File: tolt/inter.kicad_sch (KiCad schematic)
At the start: 51 parts, among them U2 L6491, U3 L6491, U4 L6491

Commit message: yaaaaaaa
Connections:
- net GND: no longer C15.2, C17.2, C19.2
- net Ph_a: now also C15.2
- net Ph_b: now also C17.2
- net Ph_c: now also C19.2

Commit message: some fixed and edit
tbd : phase voltage sensing and adct1 wiring and add on/off switch
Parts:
- D1, D2, D3: now not fitted
- R1, R2, R3: now fitted
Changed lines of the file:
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@@
 		(in_bom yes)
 		(on_board yes)
-		(dnp yes)
+		(dnp no)
 		(fields_autoplaced yes)
 		(property "Reference" "R1"
@@
 		(in_bom yes)
 		(on_board yes)
-		(dnp yes)
+		(dnp no)
 		(fields_autoplaced yes)
 		(property "Reference" "R3"
@@
 		(in_bom yes)
 		(on_board yes)
-		(dnp no)
+		(dnp yes)
 		(fields_autoplaced yes)
 		(property "Reference" "D3"
@@
 		(in_bom yes)
 		(on_board yes)
-		(dnp no)
+		(dnp yes)
 		(fields_autoplaced yes)
 		(property "Reference" "D2"
@@
 		(in_bom yes)
 		(on_board yes)
-		(dnp yes)
+		(dnp no)
 		(fields_autoplaced yes)
 		(property "Reference" "R2"
@@
 		(in_bom yes)
 		(on_board yes)
-		(dnp no)
+		(dnp yes)
 		(fields_autoplaced yes)
 		(property "Reference" "D1"

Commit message: idk just pushed for github profile lol
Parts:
- added TP1, TP2, TP3, TP4, TP5, TP6, TP7, TP8, TP9: TestPoint, symbol Connector:TestPoint
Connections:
- net H_A: now also TP3.1
- net H_B: now also TP2.1
- net H_C: now also TP5.1
- net L_A: now also TP4.1
- net L_B: now also TP1.1
- net L_C: now also TP6.1
- net SENS_A+: now also TP9.1
- net SENS_B+: now also TP8.1
- net SENS_C+: now also TP7.1

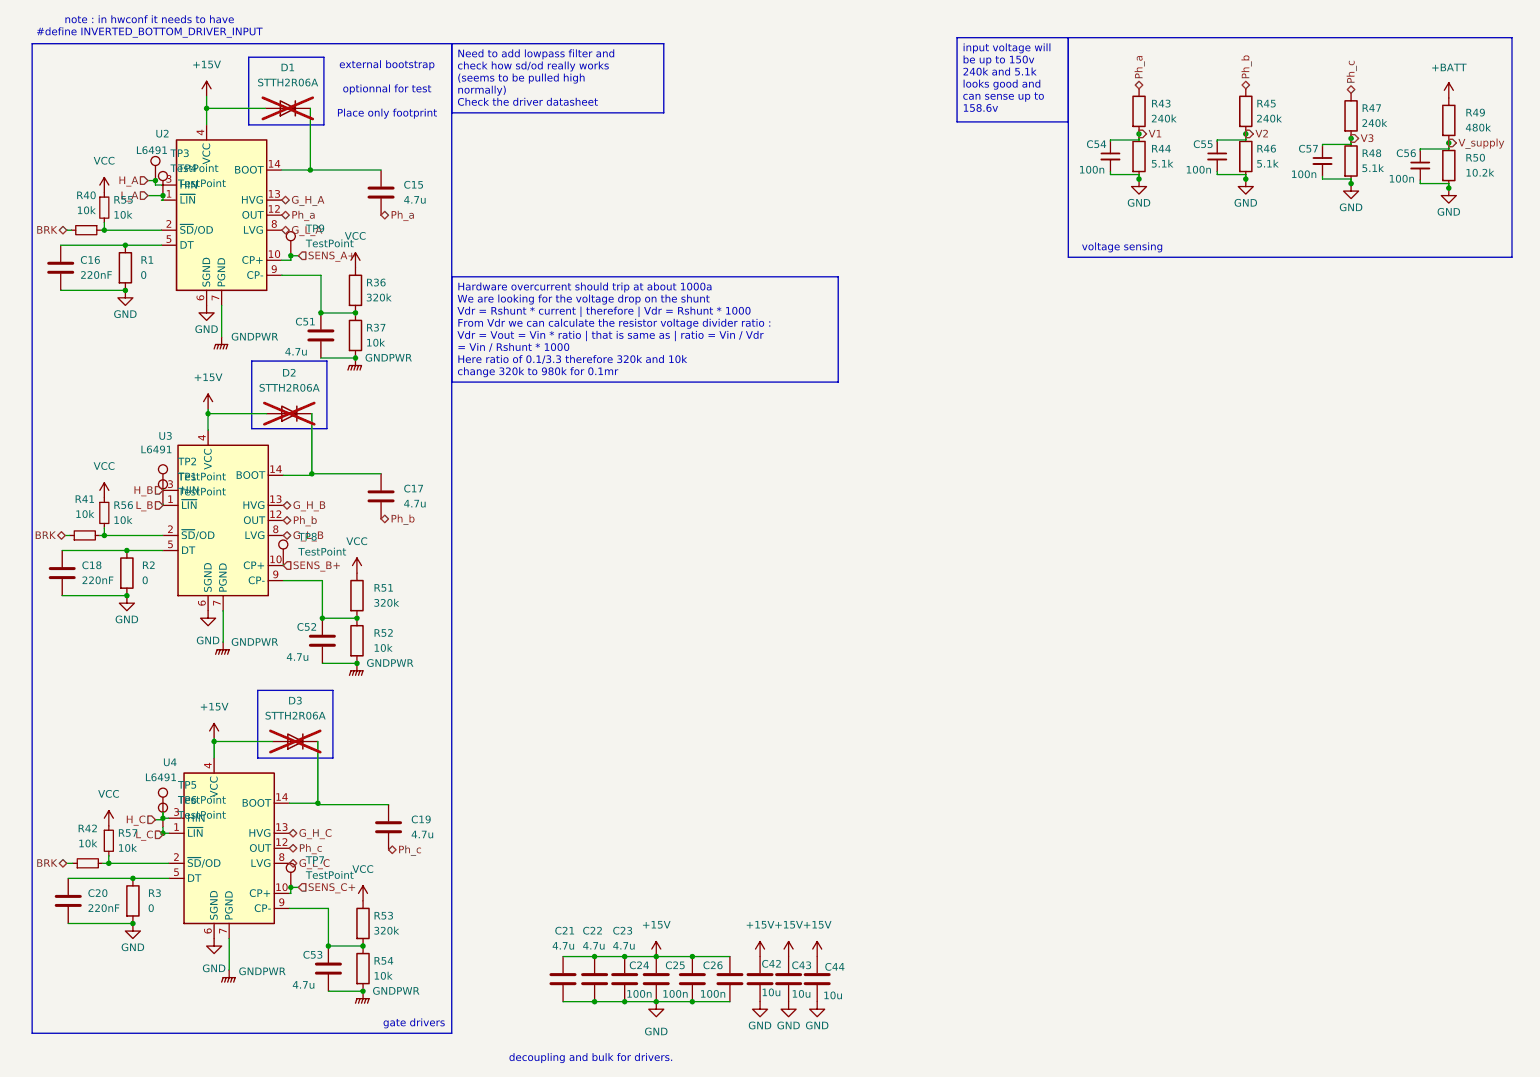
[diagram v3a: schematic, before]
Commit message: big update
fixed decoupling correctly
more gnd plane work and routing finished
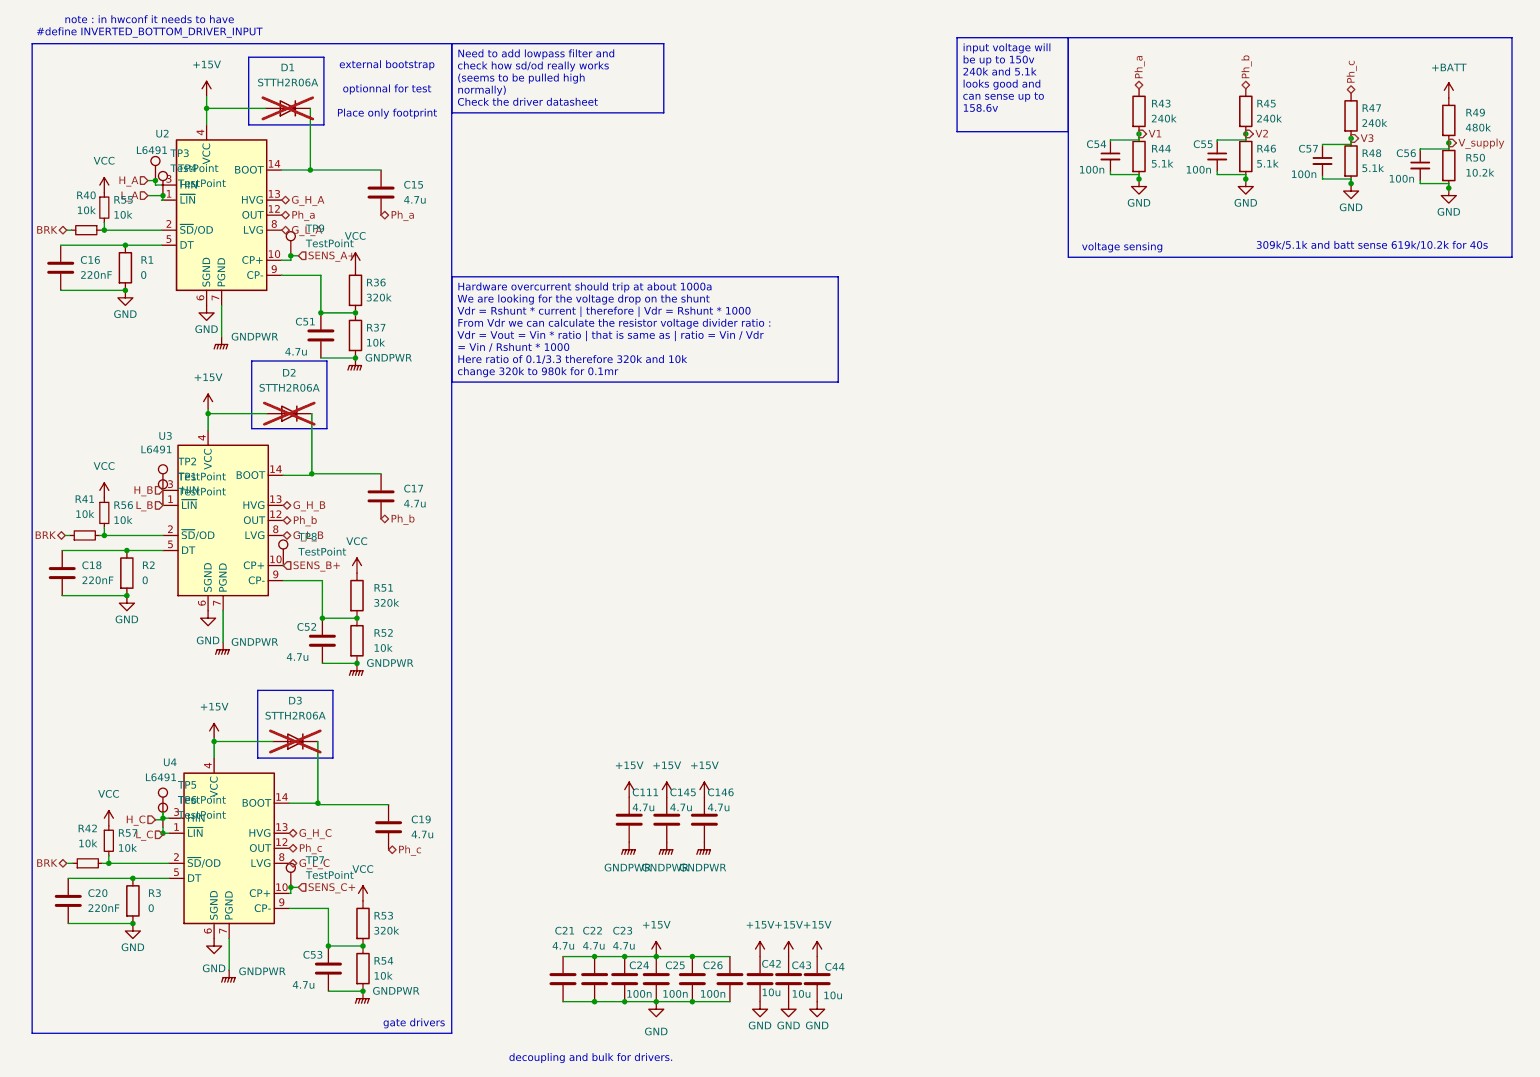
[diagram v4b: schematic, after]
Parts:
- added C111, C145, C146: 4.7u, Capacitor_SMD:C_0805_2012Metric, symbol Device:C
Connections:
- net +15V: now also C111.2, C145.2, C146.2
- net GNDPWR: now also C111.1, C145.1, C146.1
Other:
- note added: "309k/5.1k and batt sense 619k/10.2k for 40s"

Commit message: begenning of lcsc part assign
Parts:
- C42, C43, C44: footprint Capacitor_SMD:C_1210_3225Metric_Pad1.33x2.70mm_HandSolder -> Capacitor_SMD:C_1210_3225Metric
- R37, R52, R54: LCSC (none) -> C25804
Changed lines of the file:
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@@
 			)
 		)
-		(property "Footprint" "Capacitor_SMD:C_1210_3225Metric_Pad1.33x2.70mm_HandSolder"
+		(property "Footprint" "Capacitor_SMD:C_1210_3225Metric"
 			(at 156.1592 181.864 0)
 			(effects
@@
 			)
 		)
+		(property "LCSC" "C25804"
+			(at 83.312 176.276 0)
+			(effects
+				(font
+					(size 1.27 1.27)
+				)
+				(hide yes)
+			)
+		)
 		(pin "2"
 		)
@@
 			)
 		)
-		(property "Footprint" "Capacitor_SMD:C_1210_3225Metric_Pad1.33x2.70mm_HandSolder"
+		(property "Footprint" "Capacitor_SMD:C_1210_3225Metric"
 			(at 160.9852 181.864 0)
 			(effects
@@
 			)
 		)
+		(property "LCSC" "C25804"
+			(at 82.296 120.904 0)
+			(effects
+				(font
+					(size 1.27 1.27)
+				)
+				(hide yes)
+			)
+		)
 		(pin "2"
 		)
@@
 			)
 		)
+		(property "LCSC" "C25804"
+			(at 82.042 69.342 0)
+			(effects
+				(font
+					(size 1.27 1.27)
+				)
+				(hide yes)
+			)
+		)
 		(pin "2"
 		)
@@
 			)
 		)
-		(property "Footprint" "Capacitor_SMD:C_1210_3225Metric_Pad1.33x2.70mm_HandSolder"
+		(property "Footprint" "Capacitor_SMD:C_1210_3225Metric"
 			(at 151.3332 181.864 0)
 			(effects

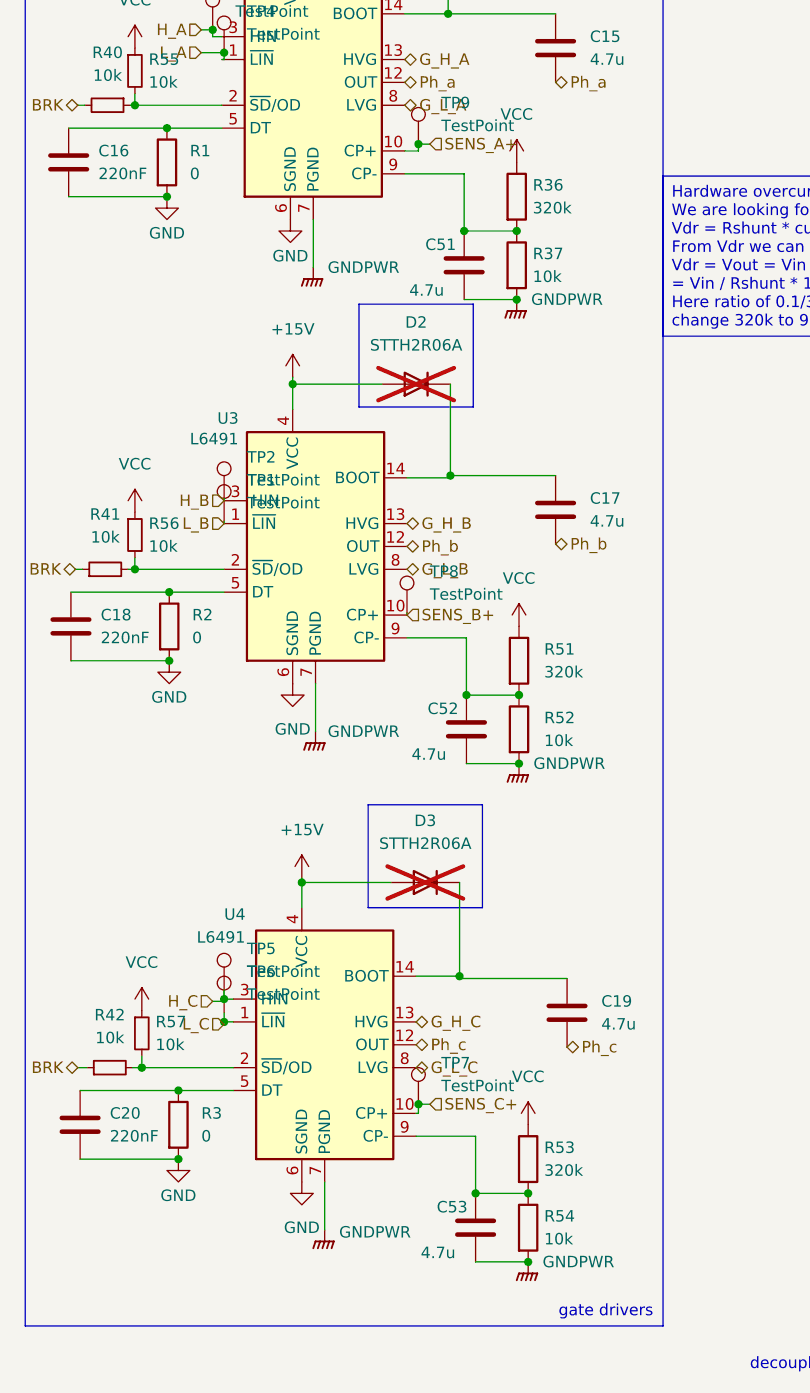
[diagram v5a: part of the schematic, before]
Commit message: more assign+12-5v change
changed with TPS82130
Since using esp32 will increase consumption by a lot
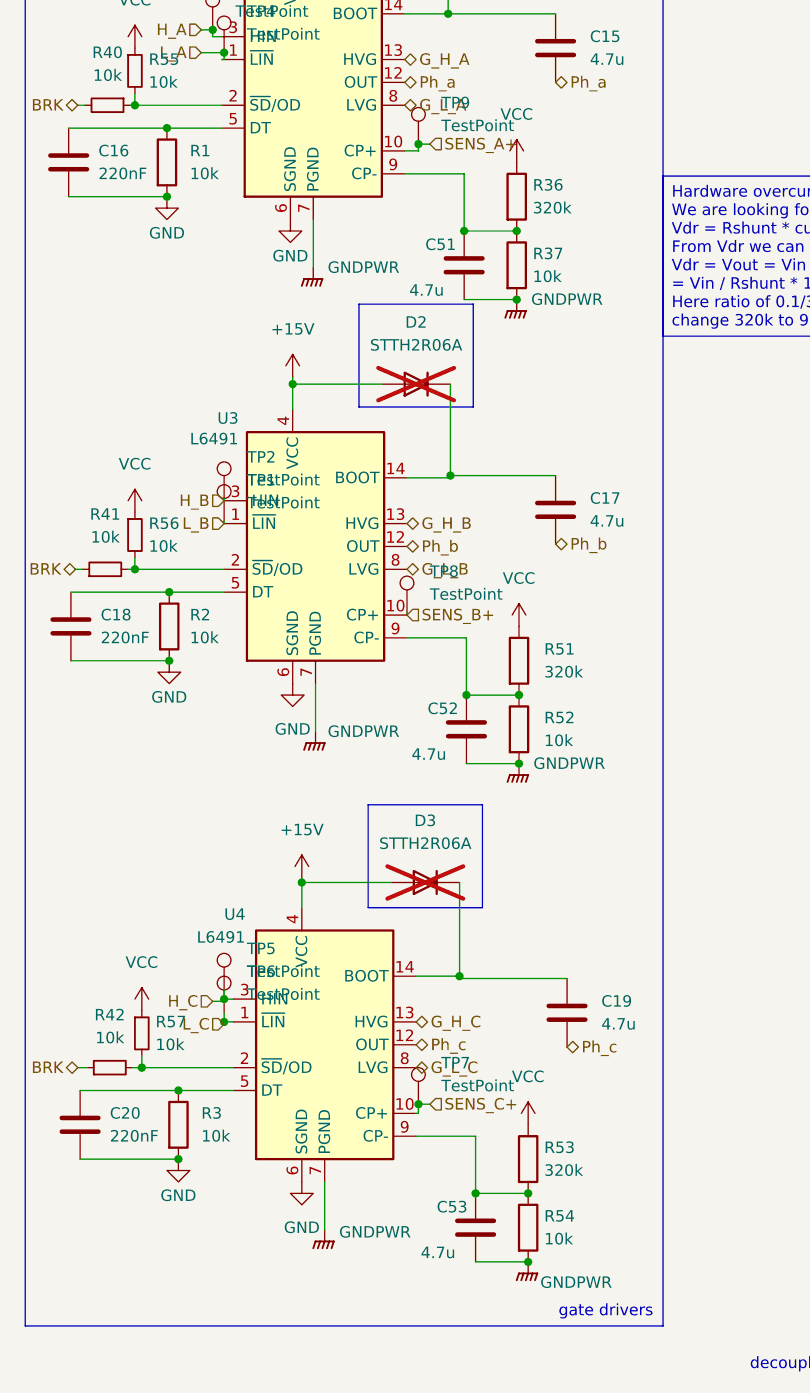
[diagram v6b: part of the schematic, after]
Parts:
- R1, R2, R3: value 0 -> 10k
- U2, U3, U4: LCSC (none) -> C2970144
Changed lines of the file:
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@@
 			)
 		)
+		(property "LCSC" "C2970144"
+			(at 59.436 49.022 0)
+			(effects
+				(font
+					(size 1.27 1.27)
+				)
+				(hide yes)
+			)
+		)
 		(pin "10"
 		)
@@
 			)
 		)
-		(property "Value" "0"
+		(property "Value" "10k"
 			(at 45.72 59.1819 0)
 			(effects
@@
 			)
 		)
-		(property "Value" "0"
+		(property "Value" "10k"
 			(at 46.99 166.1159 0)
 			(effects
@@
 			)
 		)
+		(property "LCSC" "C2970144"
+			(at 60.706 155.956 0)
+			(effects
+				(font
+					(size 1.27 1.27)
+				)
+				(hide yes)
+			)
+		)
 		(pin "10"
 		)
@@
 			)
 		)
+		(property "LCSC" "C2970144"
+			(at 59.69 100.584 0)
+			(effects
+				(font
+					(size 1.27 1.27)
+				)
+				(hide yes)
+			)
+		)
 		(pin "10"
 		)
@@
 		)
 		(property "Value" "GNDPWR"
-			(at 88.9 180.086 0)
+			(at 88.646 182.372 0)
 			(effects
 				(font
@@
 		(fields_autoplaced yes)
 		(property "Reference" "R2"
-			(at 45.974 108.2039 0)
+			(at 45.72 108.2039 0)
 			(effects
 				(font
@@
 			)
 		)
-		(property "Value" "0"
-			(at 45.974 110.7439 0)
+		(property "Value" "10k"
+			(at 45.72 110.7439 0)
 			(effects
 				(font

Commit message: hm
weird huh it didnt fucking save
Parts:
- C111, C145, C146, C15, C17, C19, C21, C22, C23: LCSC (none) -> C98192
- C16, C18, C20: LCSC (none) -> C64705
- C24, C25, C26: LCSC (none) -> C60474
- C42, C43, C44: LCSC (none) -> C138687
- C51, C52, C53: LCSC (none) -> C1705
- C54, C55, C56, C57: LCSC (none) -> C14663
- D1, D2, D3: LCSC (none) -> C50432
- R1, R2, R3: LCSC (none) -> C25804
- R36, R51, R53: LCSC (none) -> C20165692
- R37, R52, R54: LCSC C25804 -> C20165692

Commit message: Done
hopefully finished ?
needs sanity check and more checks
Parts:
- R43, R45, R47: LCSC (none) -> C870571
- R44, R46, R48: LCSC (none) -> C122969
- R49: value 480k -> 470k; LCSC (none) -> C2692714
- R50: LCSC (none) -> C4303159
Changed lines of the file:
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@@
 			)
 		)
+		(property "LCSC" "C122969"
+			(at 214.376 39.116 0)
+			(effects
+				(font
+					(size 1.27 1.27)
+				)
+				(hide yes)
+			)
+		)
 		(pin "2"
 		)
@@
 			)
 		)
+		(property "LCSC" "C870571"
+			(at 250.19 32.258 0)
+			(effects
+				(font
+					(size 1.27 1.27)
+				)
+				(hide yes)
+			)
+		)
 		(pin "2"
 		)
@@
 			)
 		)
+		(property "LCSC" "C870571"
+			(at 214.376 31.496 0)
+			(effects
+				(font
+					(size 1.27 1.27)
+				)
+				(hide yes)
+			)
+		)
 		(pin "2"
 		)
@@
 			)
 		)
+		(property "LCSC" "C4303159"
+			(at 266.7 40.64 0)
+			(effects
+				(font
+					(size 1.27 1.27)
+				)
+				(hide yes)
+			)
+		)
 		(pin "2"
 		)
@@
 			)
 		)
-		(property "Value" "480k"
+		(property "Value" "470k"
 			(at 269.494 34.2899 0)
 			(effects
@@
 			)
 		)
+		(property "LCSC" "C2692714"
+			(at 266.7 33.02 0)
+			(effects
+				(font
+					(size 1.27 1.27)
+				)
+				(hide yes)
+			)
+		)
 		(pin "2"
 		)
@@
 			)
 		)
+		(property "LCSC" "C122969"
+			(at 232.41 39.116 0)
+			(effects
+				(font
+					(size 1.27 1.27)
+				)
+				(hide yes)
+			)
+		)
 		(pin "2"
 		)
@@
 			)
 		)
+		(property "LCSC" "C122969"
+			(at 250.19 39.878 0)
+			(effects
+				(font
+					(size 1.27 1.27)
+				)
+				(hide yes)
+			)
+		)
 		(pin "2"
 		)
@@
 			(at 232.41 31.496 0)
 			(effects
+				(font
+					(size 1.27 1.27)
+				)
+				(hide yes)
+			)
+		)
+		(property "LCSC" "C870571"
+			(at 232.41 31.496 0)
+			(effects
